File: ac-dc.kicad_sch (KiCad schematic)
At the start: 55 parts, among them T1 750817251, U1 LT3799EMSE-PBF, U2 MP9989GV-Z, U3 LMR36006BRNXT

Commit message: simulation
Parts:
- C1: Part Number (none) -> 732-5733-ND
- C10, C11: Part Number (none) -> UBT1J331MHD8-ND
- C2: Part Number (none) -> 732-890414025003CS-ND
- C20: Part Number (none) -> BC3229-ND
- C3: Part Number (none) -> 732-9289-1-ND
- C6, C7: Part Number (none) -> -
- D3: Part Number (none) -> 118-CD-DF406SLCT-ND

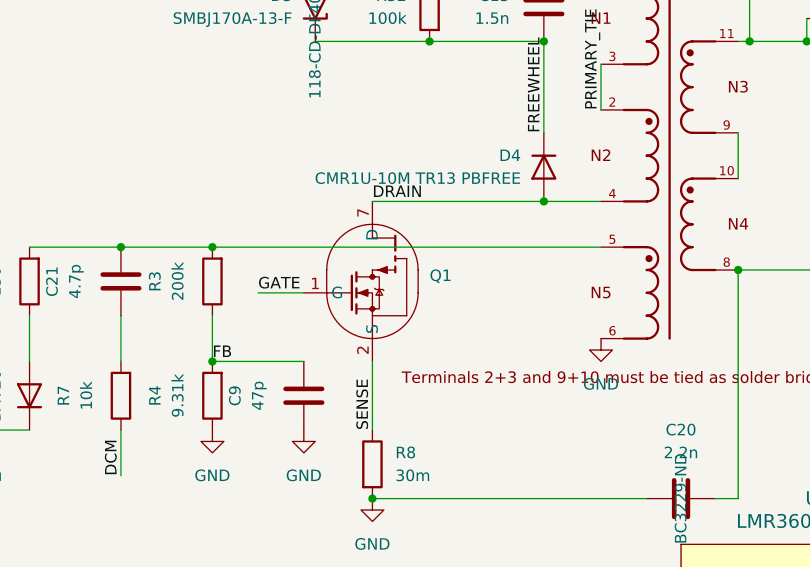
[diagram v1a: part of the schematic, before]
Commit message: new FET
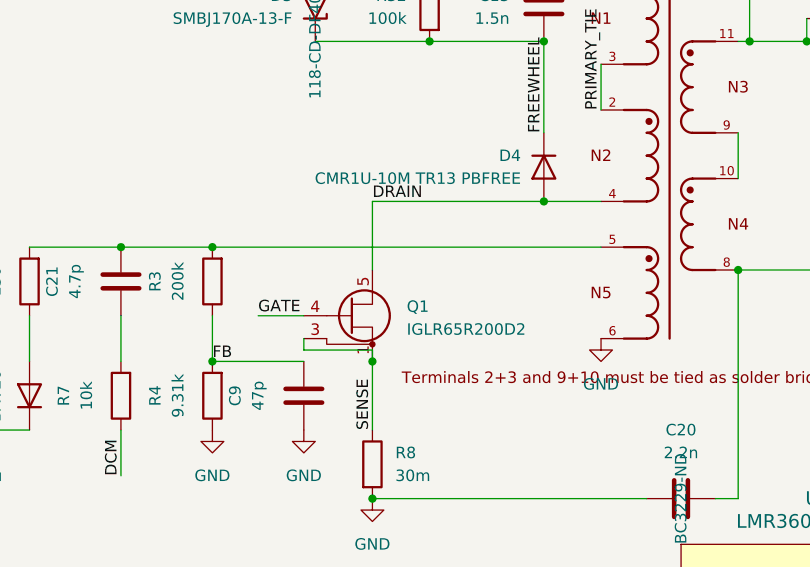
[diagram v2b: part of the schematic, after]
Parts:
- removed Q1: ~, GAN039-650NTB:GAN039-650NTB, symbol GAN039-650NTB:GAN039-650NTB
- added Q1: IGLR65R200D2, PG-TSON-8-8:PG-TSON-8-8, symbol 2025-04-05_10-38-24:IGLR65R200D2
- R25: footprint Resistor_SMD:R_1206_3216Metric -> Resistor_SMD:R_0603_1608Metric
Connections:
- net DRAIN: now also Q1.5 (D), Q1.6 (D), Q1.7 (D), Q1.8 (D)
- net GATE: now also Q1.4 (G)
- net SENSE: now also Q1.1 (S), Q1.2 (S), Q1.3 (SS), Q1.9 (S)
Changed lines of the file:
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@@
 	)
 	(junction
+		(at 152.4 93.98)
+		(diameter 0)
+		(color 0 0 0 0)
+	)
+	(junction
 		(at 165.1 119.38)
 		(diameter 0)
@@
 	(wire
 		(pts
-			(xy 139.7 86.36) (xy 144.78 86.36)
+			(xy 139.7 88.9) (xy 144.78 88.9)
 		)
 		(stroke
@@
 	(wire
 		(pts
+			(xy 152.4 92.71) (xy 152.4 93.98)
+		)
+		(stroke
+			(width 0)
+			(type default)
+		)
+	)
+	(wire
+		(pts
 			(xy 119.38 144.78) (xy 132.08 144.78)
 		)
@@
 	(wire
 		(pts
+			(xy 152.4 76.2) (xy 152.4 83.82)
+		)
+		(stroke
+			(width 0)
+			(type default)
+		)
+	)
+	(wire
+		(pts
 			(xy 119.38 139.7) (xy 132.08 139.7)
 		)
@@
 	(wire
 		(pts
+			(xy 144.78 91.44) (xy 144.78 92.71)
+		)
+		(stroke
+			(width 0)
+			(type default)
+		)
+	)
+	(wire
+		(pts
 			(xy 198.12 50.8) (xy 200.66 50.8)
 		)
@@
 	(wire
 		(pts
+			(xy 144.78 92.71) (xy 152.4 92.71)
+		)
+		(stroke
+			(width 0)
+			(type default)
+		)
+	)
+	(wire
+		(pts
 			(xy 25.4 72.39) (xy 25.4 90.17)
 		)
@@
 	)
 	(label "GATE"
-		(at 139.7 86.36 0)
+		(at 139.7 88.9 0)
 		(effects
 			(font
@@
 	)
 	(symbol
-		(lib_id "GAN039-650NTB:GAN039-650NTB")
-		(at 144.78 81.28 0)
-		(unit 1)
-		(exclude_from_sim no)
-		(in_bom yes)
-		(on_board yes)
-		(dnp no)
-		(fields_autoplaced yes)
-		(property "Reference" "Q1"
-			(at 158.75 84.4549 0)
-			(effects
-				(font
-					(size 1.27 1.27)
-				)
-				(justify left)
-			)
-		)
-		(property "Value" "~"
-			(at 158.75 86.36 0)
-			(effects
-				(font
-					(size 1.27 1.27)
-				)
-				(justify left)
-			)
-		)
-		(property "Footprint" "GAN039-650NTB:GAN039-650NTB"
-			(at 144.78 81.28 0)
-			(effects
-				(font
-					(size 1.27 1.27)
-				)
-				(hide yes)
-			)
-		)
-		(property "Datasheet" "https://assets.nexperia.com/documents/data-sheet/GAN039-650NTB.pdf"
-			(at 144.78 81.28 0)
-			(effects
-				(font
-					(size 1.27 1.27)
-				)
-				(hide yes)
-			)
-		)
-		(property "Description" ""
-			(at 144.78 81.28 0)
-			(effects
-				(font
-					(size 1.27 1.27)
-				)
-				(hide yes)
-			)
-		)
-		(property "Part Number" ""
-			(at 144.78 81.28 0)
-			(effects
-				(font
-					(size 1.27 1.27)
-				)
-			)
-		)
-		(pin "7"
-		)
-		(pin "11"
-		)
-		(pin "1"
-		)
-		(pin "4"
-		)
-		(pin "5"
-		)
-		(pin "3"
-		)
-		(pin "12"
-		)
-		(pin "9"
-		)
-		(pin "2"
-		)
-		(pin "6"
-		)
-		(pin "8"
-		)
-		(pin "10"
-		)
-		(instances
-			(project ""
-				(path "/c27c9155-8dca-4b9f-ac37-1fd4cce6afa0/a91a180e-9224-4dd9-bb32-f5cf5fec0591"
-					(reference "Q1")
-					(unit 1)
-				)
-			)
-		)
-	)
-	(symbol
 		(lib_id "Device:C")
 		(at 198.12 46.99 0)
@@
 	)
 	(symbol
+		(lib_id "2025-04-05_10-38-24:IGLR65R200D2")
+		(at 149.86 88.9 0)
+		(unit 1)
+		(exclude_from_sim no)
+		(in_bom yes)
+		(on_board yes)
+		(dnp no)
+		(fields_autoplaced yes)
+		(property "Reference" "Q1"
+			(at 156.21 87.8839 0)
+			(effects
+				(font
+					(size 1.27 1.27)
+				)
+				(justify left)
+			)
+		)
+		(property "Value" "IGLR65R200D2"
+			(at 156.21 90.4239 0)
+			(effects
+				(font
+					(size 1.27 1.27)
+				)
+				(justify left)
+			)
+		)
+		(property "Footprint" "PG-TSON-8-8:PG-TSON-8-8"
+			(at 154.94 90.805 0)
+			(effects
+				(font
+					(size 1.27 1.27)
+					(italic yes)
+				)
+				(justify left)
+				(hide yes)
+			)
+		)
+		(property "Datasheet" "https://www.infineon.com/dgdl/Infineon-IGLR65R200D2-DataSheet-v01_00-EN.pdf?fileId=8ac78c8c8eeb092c018f0a2bd2ac726f"
+			(at 154.94 92.71 0)
+			(effects
+				(font
+					(size 1.27 1.27)
+				)
+				(justify left)
+				(hide yes)
+			)
+		)
+		(property "Description" "9.2A Id, 650V Vds, 200mOhm, N-Channel GaN MOSFET, TSON-8"
+			(at 149.86 88.9 0)
+			(effects
+				(font
+					(size 1.27 1.27)
+				)
+				(hide yes)
+			)
+		)
+		(property "Sim.Library" "IGLR65R200D2/Simulation/Infineon-CoolGaN_Transistors_650_V_G5_SPICE-SimulationModels-v01_00-EN/CoolGaN Transistor 650 V G5 - Spice.lib"
+			(at 149.86 88.9 0)
+			(effects
+				(font
+					(size 1.27 1.27)
+				)
+				(hide yes)
+			)
+		)
+		(property "Sim.Name" "IGLR65R200D2_L1"
+			(at 149.86 88.9 0)
+			(effects
+				(font
+					(size 1.27 1.27)
+				)
+				(hide yes)
+			)
+		)
+		(property "Sim.Device" "SUBCKT"
+			(at 149.86 88.9 0)
+			(effects
+				(font
+					(size 1.27 1.27)
+				)
+				(hide yes)
+			)
+		)
+		(property "Sim.Pins" "1=drain 2=gate 3=source 4=source_sense"
+			(at 149.86 88.9 0)
+			(effects
+				(font
+					(size 1.27 1.27)
+				)
+				(hide yes)
+			)
+		)
+		(pin "2"
+		)
+		(pin "7"
+		)
+		(pin "3"
+		)
+		(pin "5"
+		)
+		(pin "4"
+		)
+		(pin "6"
+		)
+		(pin "8"
+		)
+		(pin "1"
+		)
+		(pin "9"
+		)
+		(instances
+			(project ""
+				(path "/c27c9155-8dca-4b9f-ac37-1fd4cce6afa0/a91a180e-9224-4dd9-bb32-f5cf5fec0591"
+					(reference "Q1")
+					(unit 1)
+				)
+			)
+		)
+	)
+	(symbol
 		(lib_id "Device:R")
 		(at 134.62 85.09 180)
@@
 			)
 		)
-		(property "Footprint" "Resistor_SMD:R_1206_3216Metric"
+		(property "Footprint" "Resistor_SMD:R_0603_1608Metric"
 			(at 135.89 133.858 90)
 			(effects

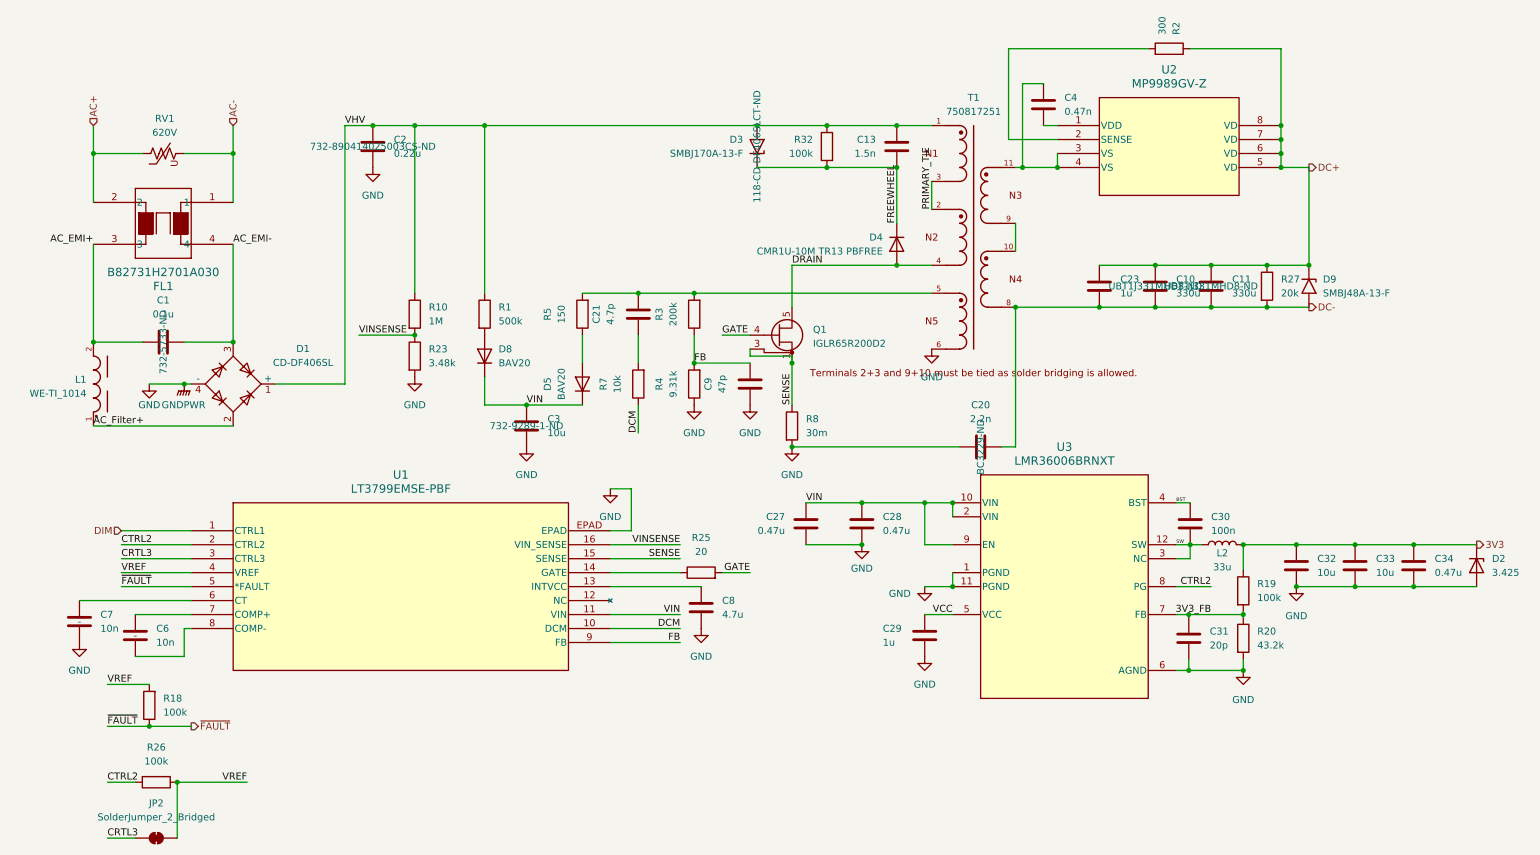
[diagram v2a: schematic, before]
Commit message: updated components
New ganfet selected and further work developing the rp2040 microcontroller circuit
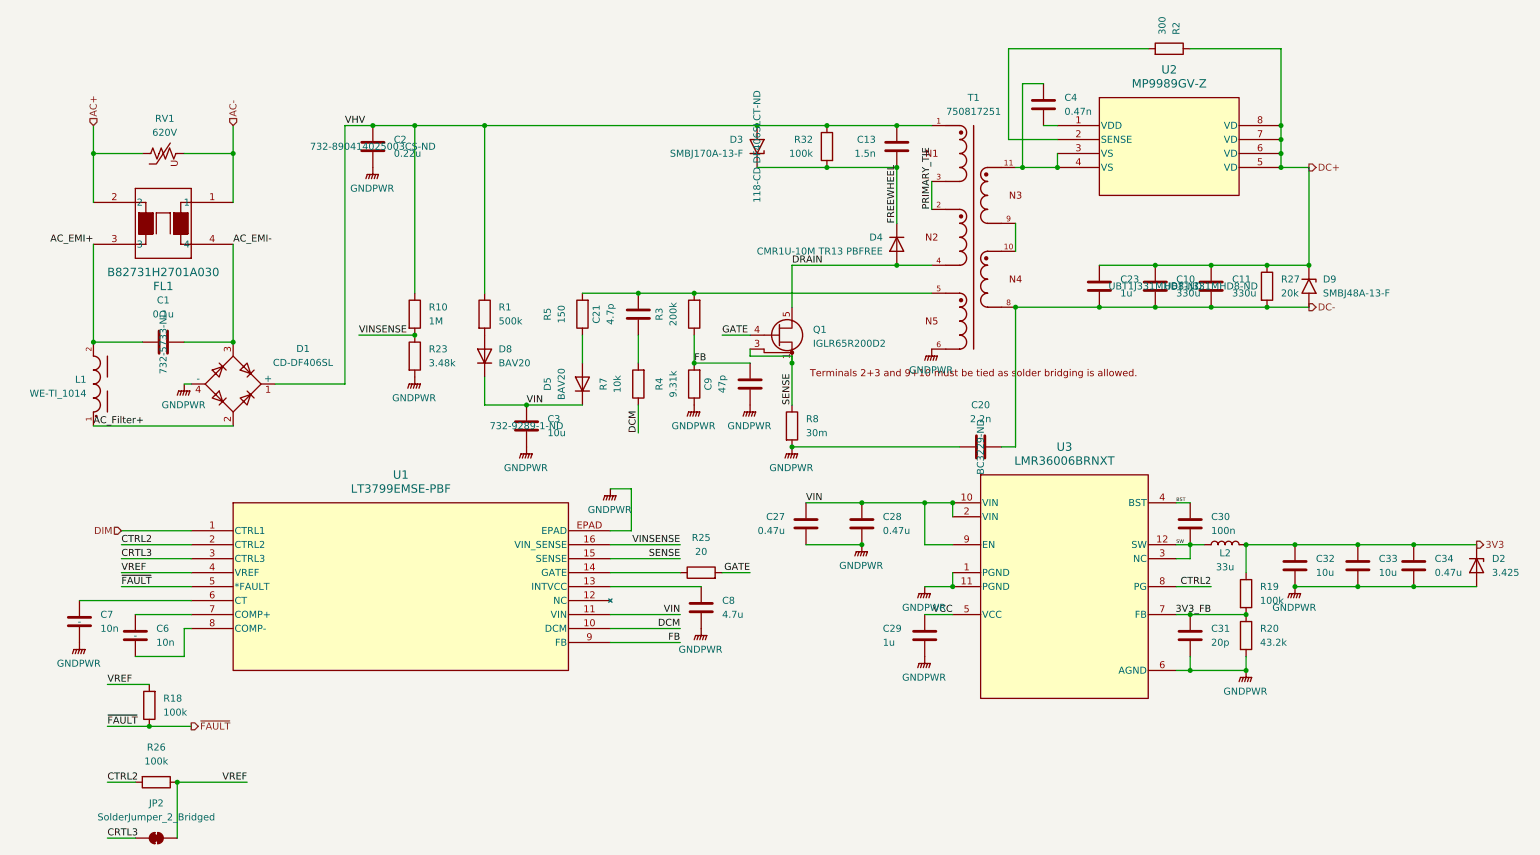
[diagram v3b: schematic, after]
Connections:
- net GND renamed GNDPWR
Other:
- moved on the sheet: C31, C33, L2, R19, R20

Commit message: finished board
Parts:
- removed C13: 1.5n, Capacitor_SMD:C_0805_2012Metric, symbol Device:C
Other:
- moved on the sheet: D4
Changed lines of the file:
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@@
 	(title_block
 		(title "Replacable LED COB Lamp")
-		(date "2025-03-24")
+		(date "2025-04-08")
 		(rev "0")
 		(company "WPI ECE2799 D25")
@@
 	)
 	(junction
-		(at 158.75 58.42)
-		(diameter 0)
-		(color 0 0 0 0)
-	)
-	(junction
 		(at 228.6 76.2)
 		(diameter 0)
@@
 	)
 	(junction
+		(at 152.4 76.2)
+		(diameter 0)
+		(color 0 0 0 0)
+	)
+	(junction
 		(at 176.53 119.38)
 		(diameter 0)
@@
 	)
 	(junction
+		(at 152.4 58.42)
+		(diameter 0)
+		(color 0 0 0 0)
+	)
+	(junction
 		(at 243.84 127)
 		(diameter 0)
@@
 	)
 	(junction
-		(at 171.45 58.42)
-		(diameter 0)
-		(color 0 0 0 0)
-	)
-	(junction
 		(at 238.76 83.82)
 		(diameter 0)
@@
 	)
 	(junction
-		(at 171.45 76.2)
-		(diameter 0)
-		(color 0 0 0 0)
-	)
-	(junction
 		(at 158.75 50.8)
 		(diameter 0)
@@
 	)
 	(junction
-		(at 171.45 50.8)
-		(diameter 0)
-		(color 0 0 0 0)
-	)
-	(junction
 		(at 96.52 50.8)
 		(diameter 0)
@@
 	(wire
 		(pts
-			(xy 158.75 58.42) (xy 171.45 58.42)
+			(xy 152.4 58.42) (xy 158.75 58.42)
 		)
 		(stroke
@@
 	(wire
 		(pts
-			(xy 171.45 50.8) (xy 177.8 50.8)
-		)
-		(stroke
-			(width 0)
-			(type default)
-		)
-	)
-	(wire
-		(pts
 			(xy 22.86 137.16) (xy 43.18 137.16)
 		)
@@
 	(wire
 		(pts
-			(xy 171.45 58.42) (xy 171.45 68.58)
+			(xy 152.4 58.42) (xy 152.4 68.58)
 		)
 		(stroke
@@
 	(wire
 		(pts
-			(xy 152.4 76.2) (xy 171.45 76.2)
+			(xy 152.4 76.2) (xy 177.8 76.2)
 		)
 		(stroke
@@
 	(wire
 		(pts
-			(xy 146.05 58.42) (xy 158.75 58.42)
+			(xy 146.05 58.42) (xy 152.4 58.42)
 		)
 		(stroke
@@
 	(wire
 		(pts
-			(xy 158.75 50.8) (xy 171.45 50.8)
+			(xy 158.75 50.8) (xy 177.8 50.8)
 		)
 		(stroke
@@
 	(wire
 		(pts
-			(xy 171.45 76.2) (xy 177.8 76.2)
-		)
-		(stroke
-			(width 0)
-			(type default)
-		)
-	)
-	(wire
-		(pts
 			(xy 243.84 127) (xy 255.27 127)
 		)
@@
 		(effects
 			(font
-				(size 1.27 1.27)
+				(size 0.635 0.635)
 			)
 			(justify left bottom)
 		)
 		(property "Netclass" "HV"
-			(at 179.07 66.04 90)
+			(at 178.7525 66.04 90)
 			(effects
 				(font
@@
 	)
 	(label "FREEWHEEL"
-		(at 171.45 68.58 90)
+		(at 152.4 68.58 90)
 		(fields_autoplaced yes)
 		(effects
@@
 		)
 		(property "Netclass" "HV"
-			(at 172.72 68.58 90)
+			(at 153.67 68.58 90)
 			(effects
 				(font
@@
 					(size 1.27 1.27)
 				)
+				(hide yes)
 			)
 		)
@@
 		(on_board yes)
 		(dnp no)
-		(fields_autoplaced yes)
 		(property "Reference" "C10"
 			(at 222.25 78.7399 0)
@@
 					(size 1.27 1.27)
 				)
+				(hide yes)
 			)
 		)
@@
 					(size 1.27 1.27)
 				)
+				(hide yes)
 			)
 		)
@@
 					(size 1.27 1.27)
 				)
+				(hide yes)
 			)
 		)
@@
 	(symbol
 		(lib_id "Device:C")
-		(at 171.45 54.61 0)
-		(mirror y)
-		(unit 1)
-		(exclude_from_sim no)
-		(in_bom yes)
-		(on_board yes)
-		(dnp no)
-		(property "Reference" "C13"
-			(at 167.64 53.3399 0)
-			(effects
-				(font
-					(size 1.27 1.27)
-				)
-				(justify left)
-			)
-		)
-		(property "Value" "1.5n"
-			(at 167.64 55.8799 0)
-			(effects
-				(font
-					(size 1.27 1.27)
-				)
-				(justify left)
-			)
-		)
-		(property "Footprint" "Capacitor_SMD:C_0805_2012Metric"
-			(at 170.4848 58.42 0)
-			(effects
-				(font
-					(size 1.27 1.27)
-				)
-				(hide yes)
-			)
-		)
-		(property "Datasheet" "~"
-			(at 171.45 54.61 0)
-			(effects
-				(font
-					(size 1.27 1.27)
-				)
-				(hide yes)
-			)
-		)
-		(property "Description" "Unpolarized capacitor"
-			(at 171.45 54.61 0)
-			(effects
-				(font
-					(size 1.27 1.27)
-				)
-				(hide yes)
-			)
-		)
-		(property "Part Number" ""
-			(at 171.45 54.61 0)
-			(effects
-				(font
-					(size 1.27 1.27)
-				)
-			)
-		)
-		(pin "1"
-		)
-		(pin "2"
-		)
-		(instances
-			(project ""
-				(path "/c27c9155-8dca-4b9f-ac37-1fd4cce6afa0/a91a180e-9224-4dd9-bb32-f5cf5fec0591"
-					(reference "C13")
-					(unit 1)
-				)
-			)
-		)
-	)
-	(symbol
-		(lib_id "Device:C")
 		(at 154.94 123.19 180)
 		(unit 1)
@@
 					(size 1.27 1.27)
 				)
+				(hide yes)
 			)
 		)
@@
 					(size 1.27 1.27)
 				)
+				(hide yes)
 			)
 		)
@@
 	(symbol
 		(lib_id "Device:D")
-		(at 171.45 72.39 90)
+		(at 152.4 72.39 90)
 		(mirror x)
 		(unit 1)
@@
 		(dnp no)
 		(property "Reference" "D4"
-			(at 168.91 71.1199 90)
+			(at 149.86 71.1199 90)
 			(effects
 				(font
@@
 		)
 		(property "Value" "CMR1U-10M TR13 PBFREE"
-			(at 168.91 73.6599 90)
+			(at 149.86 73.6599 90)
 			(effects
 				(font
@@
 		)
 		(property "Footprint" "Diode_SMD:D_SMA"
-			(at 171.45 72.39 0)
+			(at 152.4 72.39 0)
 			(effects
 				(font
@@
 		)
 		(property "Datasheet" "~"
-			(at 171.45 72.39 0)
+			(at 152.4 72.39 0)
 			(effects
 				(font
@@
 		)
 		(property "Description" "DIODE STANDARD 1000V 1A SMA"
-			(at 171.45 72.39 0)
+			(at 152.4 72.39 0)
 			(effects
 				(font
@@
 		)
 		(property "Sim.Device" "D"
-			(at 171.45 72.39 0)
+			(at 152.4 72.39 0)
 			(effects
 				(font
@@
 		)
 		(property "Sim.Pins" "1=K 2=A"
-			(at 171.45 72.39 0)
+			(at 152.4 72.39 0)
 			(effects
 				(font
@@
 		)
 		(property "Part Number" ""
-			(at 171.45 72.39 0)
+			(at 152.4 72.39 0)
 			(effects
 				(font
@@
 					(size 1.27 1.27)
 				)
+				(hide yes)
 			)
 		)

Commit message: production design files
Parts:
- C23: value 1u -> 10u; Part Number (none) -> 1276-6767-1-ND
- C27, C28, C34: Part Number (none) -> 1276-6482-1-ND
- C32, C33: Part Number (none) -> 1276-6767-1-ND
- C8: footprint Capacitor_SMD:C_0805_2012Metric -> Capacitor_SMD:C_0603_1608Metric
- D1: Part Number (none) -> 118-CD-DF406SLCT-ND
- D2: Part Number (none) -> 1727-8343-1-ND
- D3: Part Number 118-CD-DF406SLCT-ND -> 31-SMBJ170A-13-FCT-ND
- D4: Part Number (none) -> 1514-CMR1U-10MTR13PBFREECT-ND
- D5, D8: Part Number (none) -> BAV20W-FDICT-ND
- D9: Part Number (none) -> SMBJ48A-FDICT-ND
- FL1: Part Number (none) -> 495-5744-ND
- L1: Part Number (none) -> 732-4199-ND
- L2: Part Number (none) -> 732-4871-1-ND
- Q1: Part Number (none) -> 448-IGLR65R200D2XUMA1CT-ND
- R1: footprint Resistor_SMD:R_1812_4532Metric -> Resistor_SMD:R_2010_5025Metric; Part Number (none) -> 13-RC2010FK-07499KLCT-ND
- R10: Part Number (none) -> 10-ERJ-S12J105UCT-ND
- R27: Part Number (none) -> 541-4187-1-ND
- R32: footprint Resistor_SMD:R_1812_4532Metric -> Resistor_SMD:R_2010_5025Metric; Part Number (none) -> 13-RC2010JK-07100KLCT-ND
- R8: Part Number (none) -> WSLC-.03CT-ND
- RV1: Part Number (none) -> 732-13263-1-ND
- T1: Part Number (none) -> 1297-750817251-ND
- U1: Part Number (none) -> 505-LT3799EMSE#PBF-ND
- U2: Part Number (none) -> 1589-MP9989GV-ZCT-ND
- U3: Part Number (none) -> 296-53036-1-ND
